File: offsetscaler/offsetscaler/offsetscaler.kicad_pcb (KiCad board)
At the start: 2 copper layers, 55.9 x 99.1 mm, 34 parts, among them J1 IN 1, J2 OUT 1, J3 INV OUT 1, J4 EURO_PWR_2x5, J5 IN 2, J6 OUT 2, J7 INV OUT 2, U1 TL074

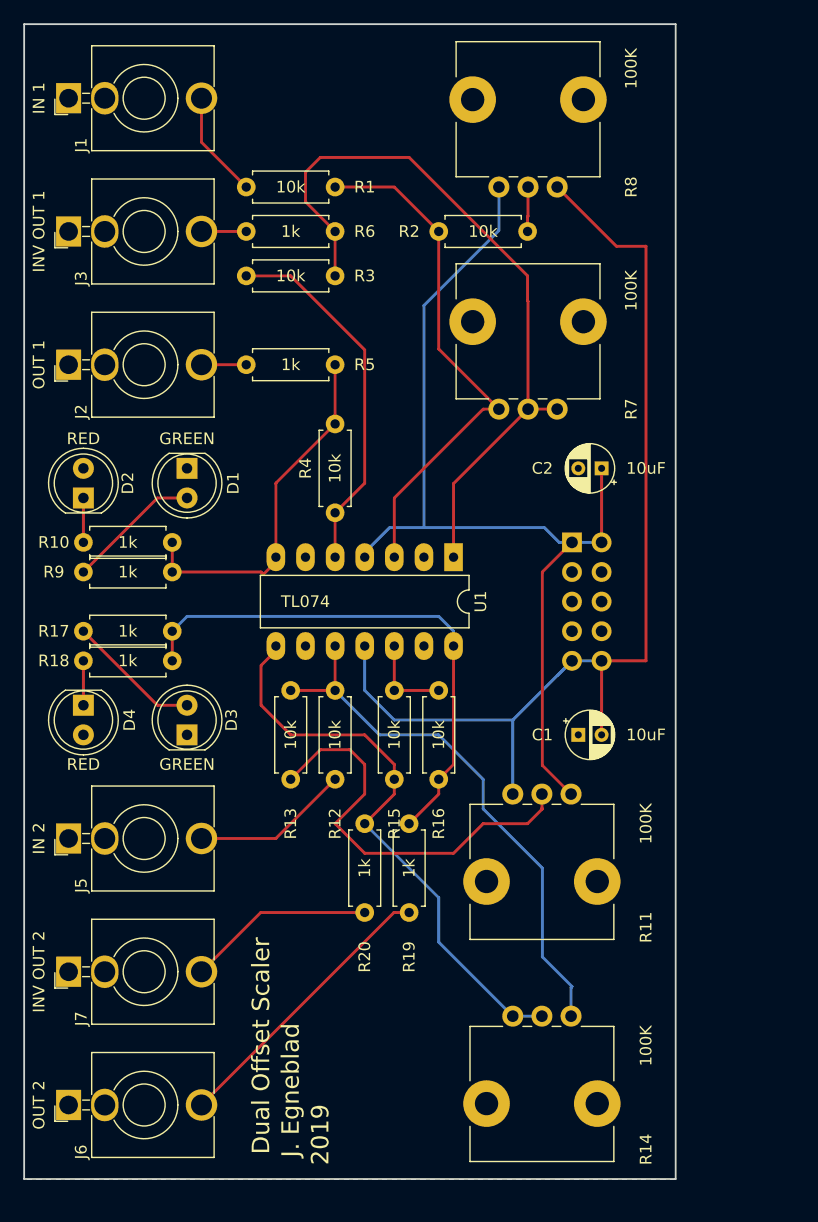
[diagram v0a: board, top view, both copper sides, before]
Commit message: Fixed offsetscaler and added some megasequencer ideas and resources
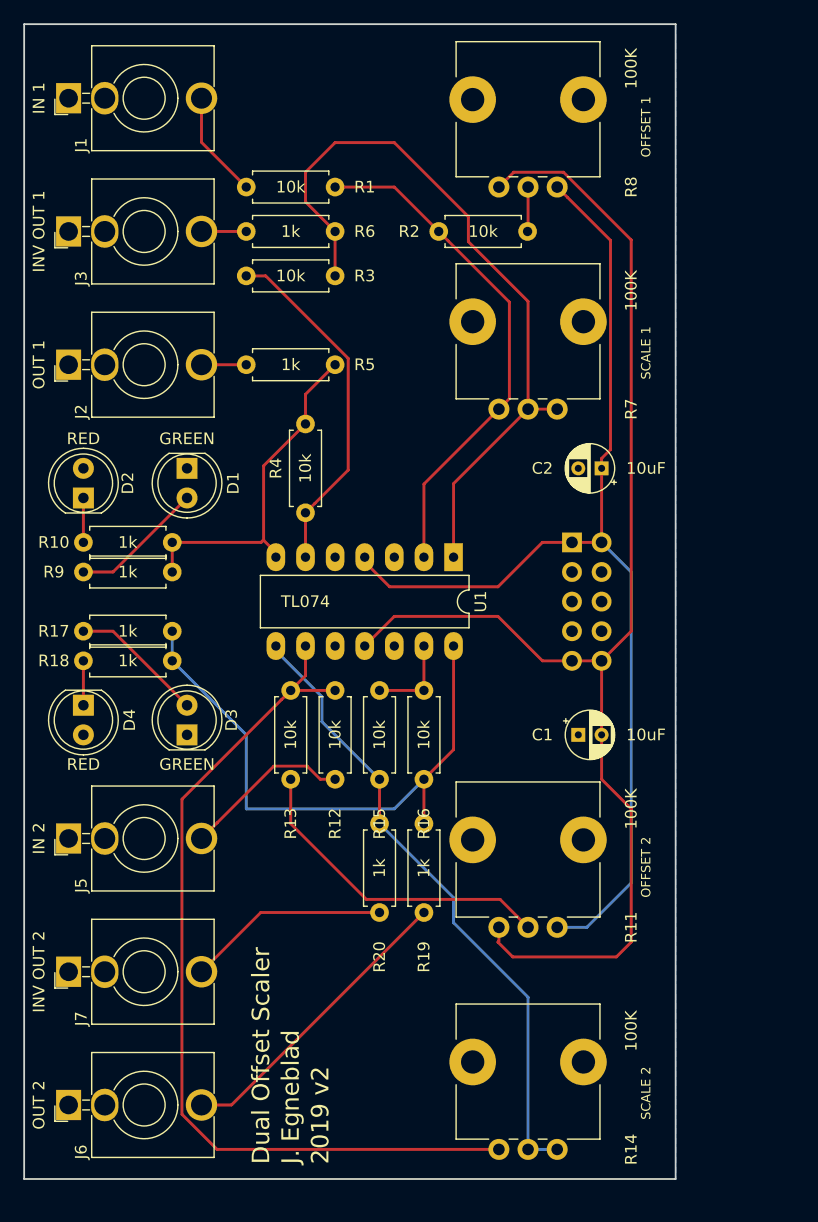
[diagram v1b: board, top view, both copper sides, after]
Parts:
- moved R11 12.0 mm to (147.3, 110.5), turned to 90 degrees
- moved R14 12.0 mm to (147.3, 129.5), turned to 90 degrees
- moved R4 2.54 mm to (125.7, 67.3)
- moved R16 1.27 mm to (135.9, 97.8)
- moved R20 1.27 mm to (132.1, 109.2)
- moved R15 1.27 mm to (132.1, 90.2)
- moved R19 1.27 mm to (135.9, 109.2)
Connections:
- R11 pad 1: -12V -> +12V
- R11 pad 3: +12V -> -12V
- R8 pad 1: -12V -> +12V
- R8 pad 3: +12V -> -12V
- U1 pad 10: Net-(R12-Pad1) -> GND
- U1 pad 12: Net-(R15-Pad1) -> GND
- U1 pad 13: GND -> Net-(R15-Pad1)
- U1 pad 2: GND -> Net-(R1-Pad1)
- U1 pad 3: Net-(R1-Pad1) -> GND
- U1 pad 5: Net-(R3-Pad1) -> GND
- U1 pad 6: GND -> Net-(R3-Pad1)
- U1 pad 9: GND -> Net-(R12-Pad1)
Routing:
- net Net-(R12-Pad1): track 47.0 -> 76.8 mm
- net -12V: track 91.3 -> 113.4 mm
- net +12V: track 84.0 -> 94.1 mm
- net Net-(R11-Pad2): track 35.8 -> 27.9 mm
- net Net-(R14-Pad1): track 49.5 -> 54.6 mm
- net Net-(R16-Pad1): track 45.8 -> 50.5 mm
- net Net-(R3-Pad1): track 31.6 -> 30.2 mm
- net Net-(J7-PadT): track 16.1 -> 17.4 mm
- net Net-(J6-PadT): track 24.6 -> 25.9 mm
- net Net-(R3-Pad2): track 63.0 -> 64.1 mm
- net Net-(R1-Pad1): track 45.0 -> 44.0 mm
- net Net-(R10-Pad2): track 31.0 -> 29.9 mm
- net Net-(J5-PadT): track 13.6 -> 14.5 mm
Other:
- board text added: "2019 v2"
- board text added: "OFFSET 1"
- board text added: "OFFSET 2"
- board text added: "SCALE 1"
- board text added: "SCALE 2"
- board text removed: "2019"

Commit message: Make the offset scaler fit the new standard
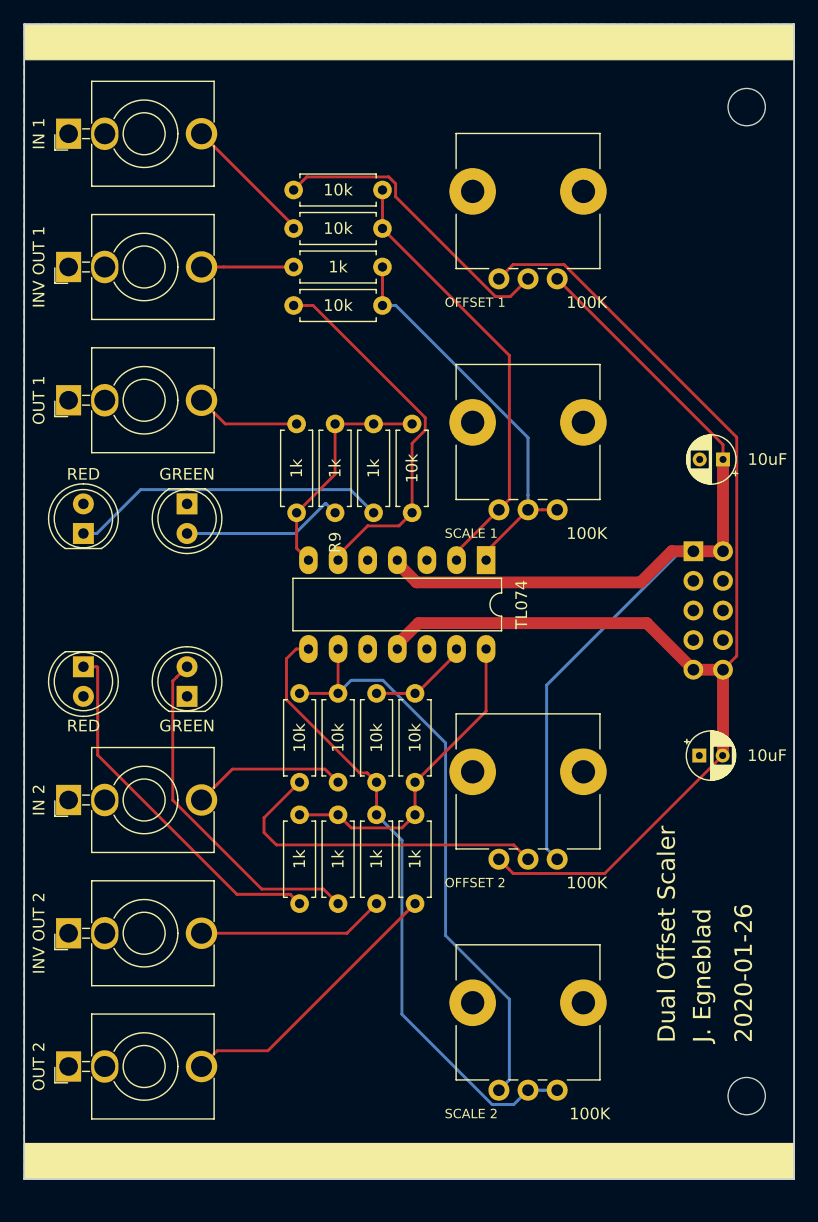
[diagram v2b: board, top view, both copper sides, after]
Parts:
- added H1: MountingHole, MountingHole:MountingHole_3.2mm_M3, F.Cu at (163.6, 40.1)
- added H2: MountingHole, MountingHole:MountingHole_3.2mm_M3, F.Cu at (163.6, 125.0)
- moved R17 32.0 mm to (128.5, 108.5), turned to 90 degrees
- moved R18 27.9 mm to (125.2, 108.5), turned to 90 degrees
- moved R10 25.0 mm to (131.6, 74.9), turned to 90 degrees
- moved R9 22.2 mm to (128.3, 74.9), turned to 90 degrees
- moved C1 10.5 mm to (159.5, 95.8)
- moved C2 10.4 mm to (161.5, 70.4)
- moved J4 10.4 mm to (159.0, 78.2)
- moved R4 9.14 mm to (134.9, 67.3)
- moved R7 8.64 mm to (147.3, 74.7)
- moved R8 7.87 mm to (147.3, 54.9)
- moved R5 6.67 mm to (125.0, 67.3), turned to 270 degrees
- moved R2 5.99 mm to (132.3, 47.2), turned to 180 degrees
- moved R11 5.84 mm to (147.3, 104.6)
- moved R1 5.40 mm to (132.3, 50.5)
- moved R14 5.08 mm to (147.3, 124.5)
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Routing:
- net Net-(R3-Pad2): track 64.1 -> 35.0 mm
- net Net-(D4-Pad1): track 3.81 -> 31.4 mm
- net Net-(R12-Pad1): track 76.8 -> 51.4 mm
- net Net-(D2-Pad1): track 3.81 -> 27.3 mm
- net Net-(R16-Pad1): track 50.5 -> 27.6 mm
- net Net-(R2-Pad2): track 3.83 -> 26.1 mm
- net Net-(D3-Pad2): track 11.5 -> 29.8 mm
- net Net-(R10-Pad2): track 29.9 -> 20.1 mm
- net Net-(R1-Pad1): track 44.0 -> 38.1 mm
- net Net-(J2-PadT): track 3.84 -> 9.00 mm
- net Net-(J3-PadT): track 3.84 -> 7.90 mm
- net -12V: track 113.4 -> 109.5 mm
- net Net-(D1-Pad2): track 11.5 -> 14.1 mm
- net Net-(J1-PadT): track 9.21 -> 11.4 mm
- net +12V: track 94.1 -> 91.9 mm
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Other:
- board size 55.9 x 99.1 mm -> 66 x 99.1 mm
- board text added: "2020-01-26"
- board text removed: "2019 v2"

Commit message: Sent off lots off stuff for etsing
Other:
- board text added: "2020-04-01"
- board text removed: "2020-01-26"
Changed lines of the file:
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@@
     (pcbplotparams
       (layerselection 0x010f0_ffffffff)
-      (usegerberextensions true)
-      (usegerberattributes false)
+      (usegerberextensions false)
+      (usegerberattributes true)
       (usegerberadvancedattributes false)
       (creategerberjobfile false)
@@
       (viasonmask false)
       (mode 1)
-      (useauxorigin false)
+      (useauxorigin true)
       (hpglpennumber 1)
       (hpglpenspeed 20)
@@
       (drillshape 0)
       (scaleselection 1)
-      (outputdirectory "gerber/"))
+      (outputdirectory "plots/"))
   )
   (net 0 "")
@@
     (descr "Resistor, Axial_DIN0207 series, Axial, Horizontal, pin pitch=7.62mm, 0.25W = 1/4W, length*diameter=6.3*2.5mm^2, http://cdn-reichelt.de/documents/datenblatt/B400/1_4W%23YAG.pdf")
     (tags "Resistor Axial_DIN0207 series Axial Horizontal pin pitch 7.62mm 0.25W = 1/4W length 6.3mm diameter 2.5mm")
-    (fp_text reference R9 (at -2.54 0 90) (layer F.SilkS)
+    (fp_text reference R9 (at -2.54 0 90) (layer F.SilkS) hide
       (effects (font (size 1 1) (thickness 0.15)))
     )
@@
     (fp_line (start 8.67 1.5) (end 8.67 -1.5) (layer F.CrtYd) (width 0.05))
     (fp_line (start 8.67 -1.5) (end -1.05 -1.5) (layer F.CrtYd) (width 0.05))
-    (fp_text user %R (at -2.54 0 90) (layer F.Fab)
+    (fp_text user %R (at -2.54 0 90) (layer F.Fab) hide
       (effects (font (size 1 1) (thickness 0.15)))
     )
@@
     (effects (font (size 0.8 0.8) (thickness 0.1)) (justify left))
   )
-  (gr_text 2020-01-26 (at 163.322 120.396 90) (layer F.SilkS)
+  (gr_text 2020-04-01 (at 163.322 120.396 90) (layer F.SilkS)
     (effects (font (size 1.5 1.5) (thickness 0.3)) (justify left))
   )
